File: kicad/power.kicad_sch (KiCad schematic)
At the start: 76 parts, among them J6 RTC Battery, U1 MIMXRT1171DVMAB, U8 TPS62086, U9 TPS62825, Y3 24MHz, Y4 32.768kHz

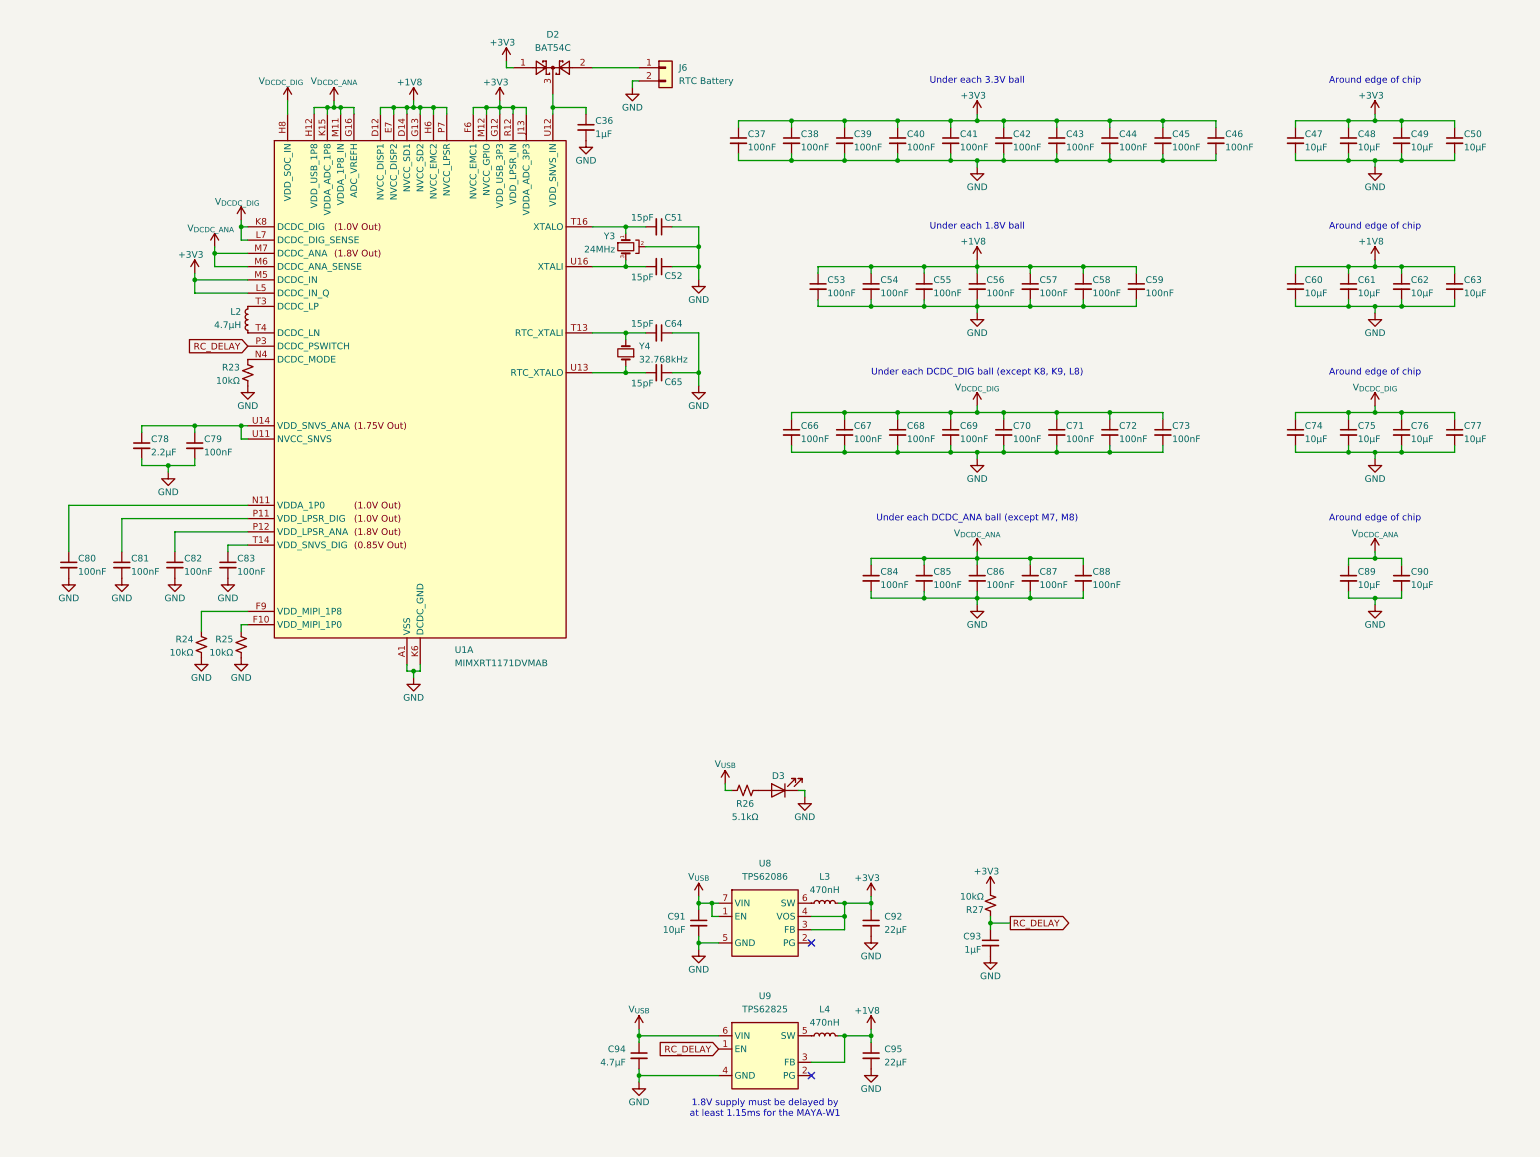
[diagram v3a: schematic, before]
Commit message: added inductor footprints
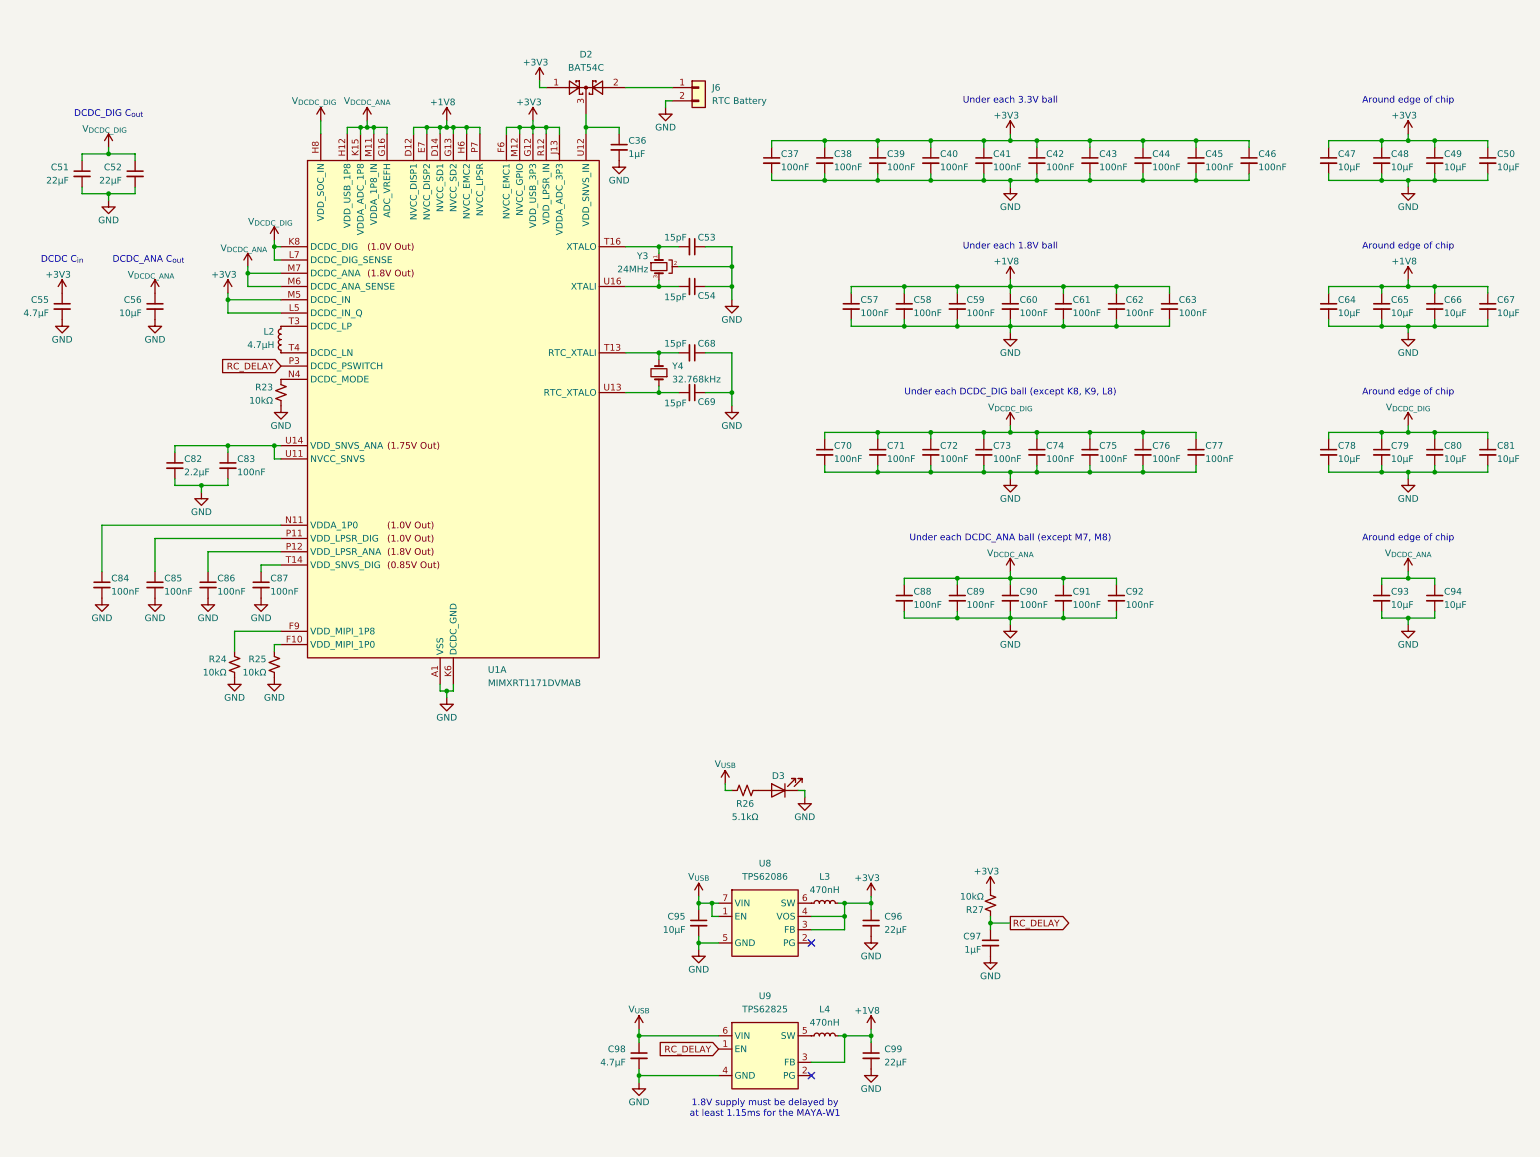
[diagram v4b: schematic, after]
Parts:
- added C51, C52: 22μF, Capacitor_SMD:C_0402_1005Metric, symbol Device:C_Small
- added C55: 4.7μF, Capacitor_SMD:C_0201_0603Metric, symbol Device:C_Small
- added C56: 10μF, Capacitor_SMD:C_0201_0603Metric, symbol Device:C_Small
- C53: renamed from C51; footprint Capacitor_SMD:C_0402_1005Metric -> Capacitor_SMD:C_0201_0603Metric
- C54: renamed from C52; footprint Capacitor_SMD:C_0402_1005Metric -> Capacitor_SMD:C_0201_0603Metric
- C60: renamed from C56; footprint Capacitor_SMD:C_0201_0603Metric -> Capacitor_SMD:C_0402_1005Metric
- C61: renamed from C57; footprint Capacitor_SMD:C_0201_0603Metric -> Capacitor_SMD:C_0402_1005Metric
- C62: renamed from C58; footprint Capacitor_SMD:C_0201_0603Metric -> Capacitor_SMD:C_0402_1005Metric
- C63: renamed from C59; footprint Capacitor_SMD:C_0201_0603Metric -> Capacitor_SMD:C_0402_1005Metric
- C66: renamed from C62; footprint Capacitor_SMD:C_0402_1005Metric -> Capacitor_SMD:C_0201_0603Metric
- C67: renamed from C63; footprint Capacitor_SMD:C_0402_1005Metric -> Capacitor_SMD:C_0201_0603Metric
- C68: renamed from C64; footprint Capacitor_SMD:C_0402_1005Metric -> Capacitor_SMD:C_0201_0603Metric
- C69: renamed from C65; footprint Capacitor_SMD:C_0402_1005Metric -> Capacitor_SMD:C_0201_0603Metric
- C74: renamed from C70; footprint Capacitor_SMD:C_0201_0603Metric -> Capacitor_SMD:C_0402_1005Metric
- C75: renamed from C71; footprint Capacitor_SMD:C_0201_0603Metric -> Capacitor_SMD:C_0402_1005Metric
- C76: renamed from C72; footprint Capacitor_SMD:C_0201_0603Metric -> Capacitor_SMD:C_0402_1005Metric
- C77: renamed from C73; footprint Capacitor_SMD:C_0201_0603Metric -> Capacitor_SMD:C_0402_1005Metric
- C78: renamed from C74; footprint Capacitor_SMD:C_0402_1005Metric -> (none)
- C79: renamed from C75; footprint Capacitor_SMD:C_0402_1005Metric -> Capacitor_SMD:C_0201_0603Metric
- C80: renamed from C76; footprint Capacitor_SMD:C_0402_1005Metric -> Capacitor_SMD:C_0201_0603Metric
- C81: renamed from C77; footprint Capacitor_SMD:C_0402_1005Metric -> Capacitor_SMD:C_0201_0603Metric
- C82: renamed from C78; footprint (none) -> Capacitor_SMD:C_0201_0603Metric
- C89: renamed from C85; footprint Capacitor_SMD:C_0201_0603Metric -> Capacitor_SMD:C_0402_1005Metric
- C90: renamed from C86; footprint Capacitor_SMD:C_0201_0603Metric -> Capacitor_SMD:C_0402_1005Metric
- C91: renamed from C87; footprint Capacitor_SMD:C_0201_0603Metric -> Capacitor_SMD:C_0402_1005Metric
- C92: renamed from C88; footprint Capacitor_SMD:C_0201_0603Metric -> (none)
- C93: renamed from C89; footprint Capacitor_SMD:C_0402_1005Metric -> (none)
- C94: renamed from C90; footprint Capacitor_SMD:C_0402_1005Metric -> (none)
- C95: renamed from C91; footprint Capacitor_SMD:C_0402_1005Metric -> (none)
- L2: footprint (none) -> project_footprints:SDCL1V4018
- L3, L4: footprint (none) -> project_footprints:L_0806
- renumbered C53 to C57, C54 to C58, C55 to C59, C60 to C64, C61 to C65, C66 to C70, C67 to C71, C68 to C72, C69 to C73, C79 to C83, C80 to C84, C81 to C85, C82 to C86, C83 to C87, C84 to C88, C92 to C96, C93 to C97, C94 to C98, C95 to C99
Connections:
- net +3V3: now also C55.1
- net GND: now also C51.2, C52.2, C55.2, C56.2
- net V_{DCDC_ANA}: now also C56.1
- net V_{DCDC_DIG}: now also C51.1, C52.1
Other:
- note added: "DCDC C_{in}"
- note added: "DCDC_ANA C_{out}"
- note added: "DCDC_DIG C_{out}"
- moved on the sheet: C36, C37, C38, C39, C40, C41, C42, C43, C44, C45, C46, C47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

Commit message: reworked bypass capacitors for MIMXRT1171DVMAB
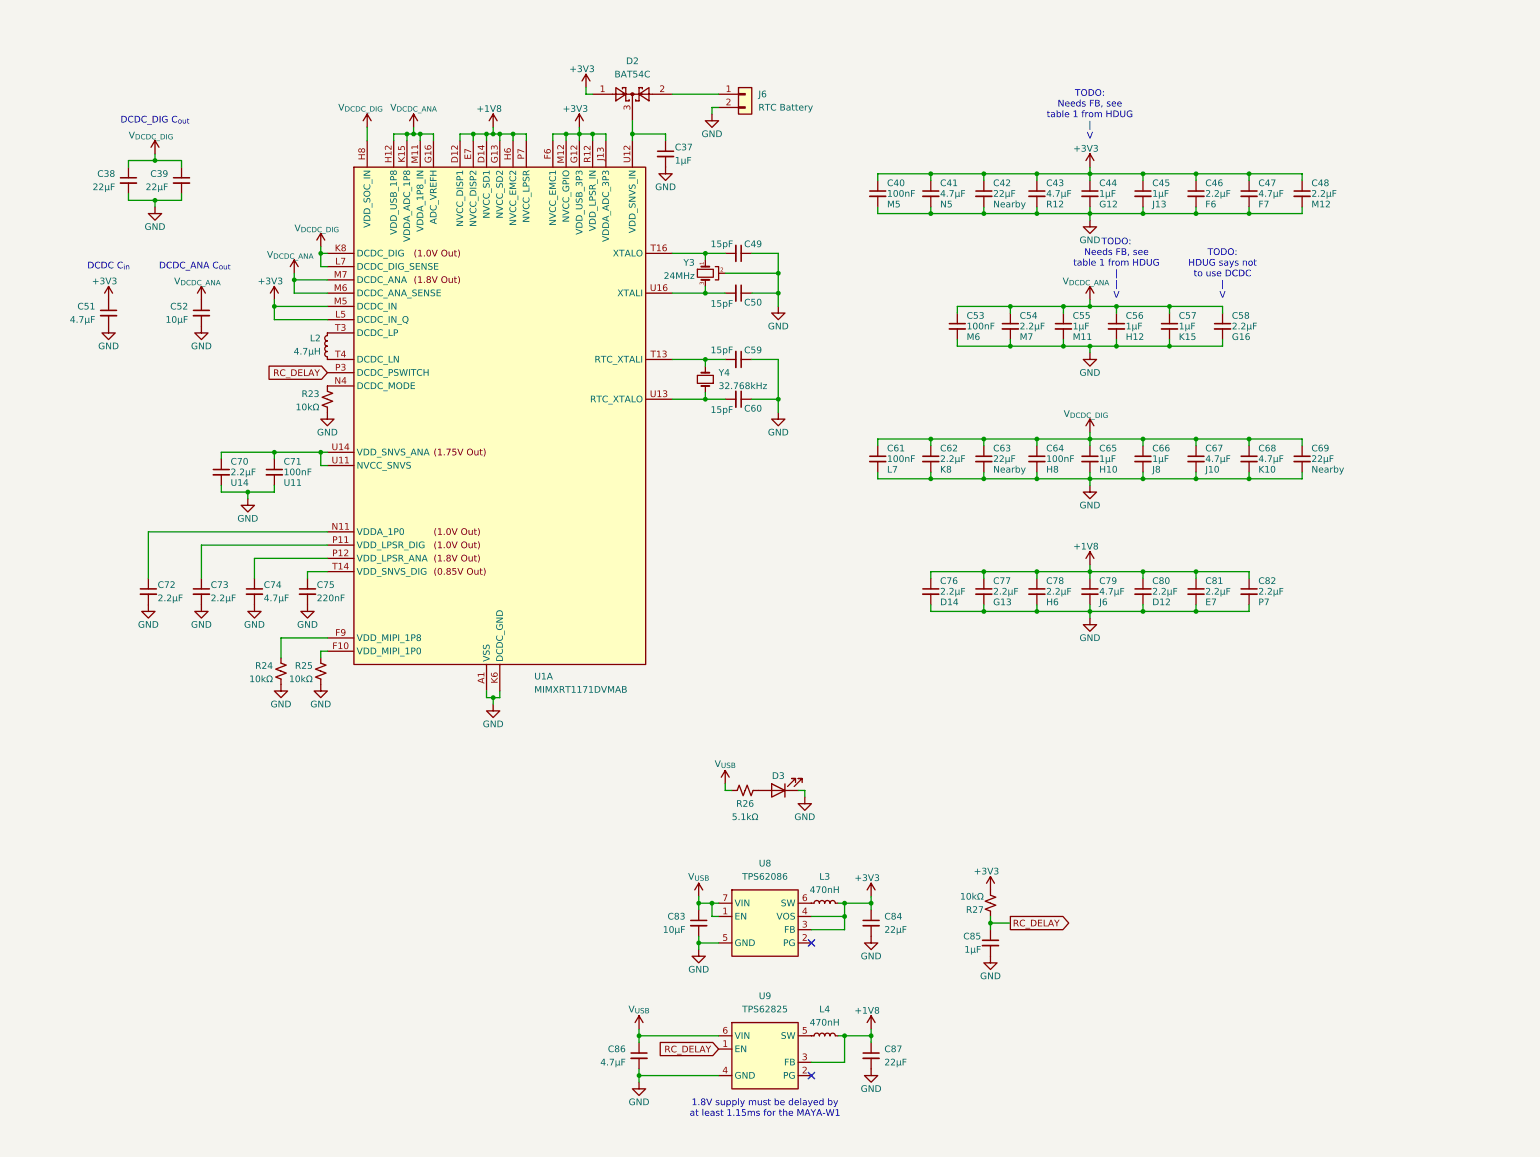
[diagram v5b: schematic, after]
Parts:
- removed C37, C38, C39, C59, C72, C83, C85, C88: 100nF, Capacitor_SMD:C_0201_0603Metric, symbol Device:C_Small
- removed C49, C50: 10μF, Capacitor_SMD:C_0402_1005Metric, symbol Device:C_Small
- removed C60, C74, C75, C89, C90, C91: 100nF, Capacitor_SMD:C_0402_1005Metric, symbol Device:C_Small
- removed C92: 100nF, symbol Device:C_Small
- removed C93, C94: 10μF, symbol Device:C_Small
- added C53: 100nF, symbol Device:C_Small
- added C54: 2.2μF, symbol Device:C_Small
- added C55, C56: 1μF, symbol Device:C_Small
- added C68: 4.7μF, symbol Device:C_Small
- added C69: 22μF, symbol Device:C_Small
- C37: renamed from C36; footprint Capacitor_SMD:C_0402_1005Metric -> (none)
- C38: renamed from C51; footprint Capacitor_SMD:C_0402_1005Metric -> (none)
- C39: renamed from C52; footprint Capacitor_SMD:C_0402_1005Metric -> (none)
- C40, C71, C82: footprint Capacitor_SMD:C_0201_0603Metric -> (none)
- C41, C43: value 100nF -> 4.7μF; footprint Capacitor_SMD:C_0201_0603Metric -> (none)
- C42: value 100nF -> 22μF; footprint Capacitor_SMD:C_0201_0603Metric -> (none)
- C44, C45, C57: value 100nF -> 1μF; footprint Capacitor_SMD:C_0201_0603Metric -> (none)
- C46, C58, C70, C73: value 100nF -> 2.2μF; footprint Capacitor_SMD:C_0201_0603Metric -> (none)
- C47: value 10μF -> 4.7μF; footprint Capacitor_SMD:C_0402_1005Metric -> (none)
- C48: value 10μF -> 2.2μF; footprint Capacitor_SMD:C_0402_1005Metric -> (none)
- C49: renamed from C53; footprint Capacitor_SMD:C_0201_0603Metric -> Capacitor_SMD:C_0402_1005Metric
- C50: renamed from C54; footprint Capacitor_SMD:C_0201_0603Metric -> Capacitor_SMD:C_0402_1005Metric
- C51: renamed from C55; footprint Capacitor_SMD:C_0201_0603Metric -> (none)
- C52: renamed from C56; footprint Capacitor_SMD:C_0201_0603Metric -> Capacitor_SMD:C_0402_1005Metric
- C59: renamed from C68; footprint Capacitor_SMD:C_0201_0603Metric -> Capacitor_SMD:C_0402_1005Metric
- C60: renamed from C69; footprint Capacitor_SMD:C_0201_0603Metric -> Capacitor_SMD:C_0402_1005Metric
- C61: footprint Capacitor_SMD:C_0402_1005Metric -> (none)
- C62, C76, C77: value 100nF -> 2.2μF; footprint Capacitor_SMD:C_0402_1005Metric -> (none)
- C63: value 100nF -> 22μF; footprint Capacitor_SMD:C_0402_1005Metric -> (none)
- C64: value 10μF -> 100nF; footprint Capacitor_SMD:C_0402_1005Metric -> (none)
- C65: value 10μF -> 1μF; footprint Capacitor_SMD:C_0402_1005Metric -> (none)
- C66: value 10μF -> 1μF; footprint Capacitor_SMD:C_0201_0603Metric -> (none)
- C67, C79: value 10μF -> 4.7μF; footprint Capacitor_SMD:C_0201_0603Metric -> (none)
- C72: renamed from C84; value 100nF -> 2.2μF
- C74: renamed from C86; value 100nF -> 4.7μF; footprint Capacitor_SMD:C_0201_0603Metric -> (none)
- C75: renamed from C87; value 100nF -> 220nF
- C78: value 10μF -> 2.2μF
- C80, C81: value 10μF -> 2.2μF; footprint Capacitor_SMD:C_0201_0603Metric -> (none)
- C83: renamed from C95; footprint (none) -> Capacitor_SMD:C_0402_1005Metric
- renumbered C96 to C84, C97 to C85, C98 to C86, C99 to C87
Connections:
- net +1V8: now also C76.1, C77.1, C78.1, C79.1, C80.1, C81.1, C82.1; no longer C57.1, C58.1, C61.1, C62.1, C63.1, C64.1, C65.1, C66.1, C67.1
- net GND: now also C53.2, C54.2, C55.2, C56.2, C68.2, C69.2
- net V_{DCDC_ANA}: now also C57.1, C58.1, C53.1, C54.1, C55.1, C56.1
- net V_{DCDC_DIG}: now also C61.1, C62.1, C63.1, C64.1, C65.1, C66.1, C67.1, C68.1, C69.1; no longer C70.1, C71.1, C73.1, C76.1, C77.1, C78.1, C79.1, C80.1, C81.1
- net at U1.P11 (VDD_LPSR_DIG): now also C73.1
- net at U1.U11 (NVCC_SNVS), U1.U14 (VDD_SNVS_ANA): now also C70.1, C71.1; no longer C82.1
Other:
- note added: "TODO: HDUG says not to use DCDC | V"
- note added: "TODO: Needs FB, see table 1 from HDUG | V"
- note added: "TODO: Needs FB, see table 1 from HDUG | | V"
- note removed: "Around edge of chip"
- note removed: "Under each 1.8V ball"
- note removed: "Under each 3.3V ball"
- note removed: "Under each DCDC_ANA ball (except M7, M8)"
- note removed: "Under each DCDC_DIG ball (except K8, K9, L8)"
- moved on the sheet: C37, C38, C39, C49, C50, C51, C52, C59, C60, C72, C74, C75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

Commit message: moved ADC_VREFH to +1V8 rail
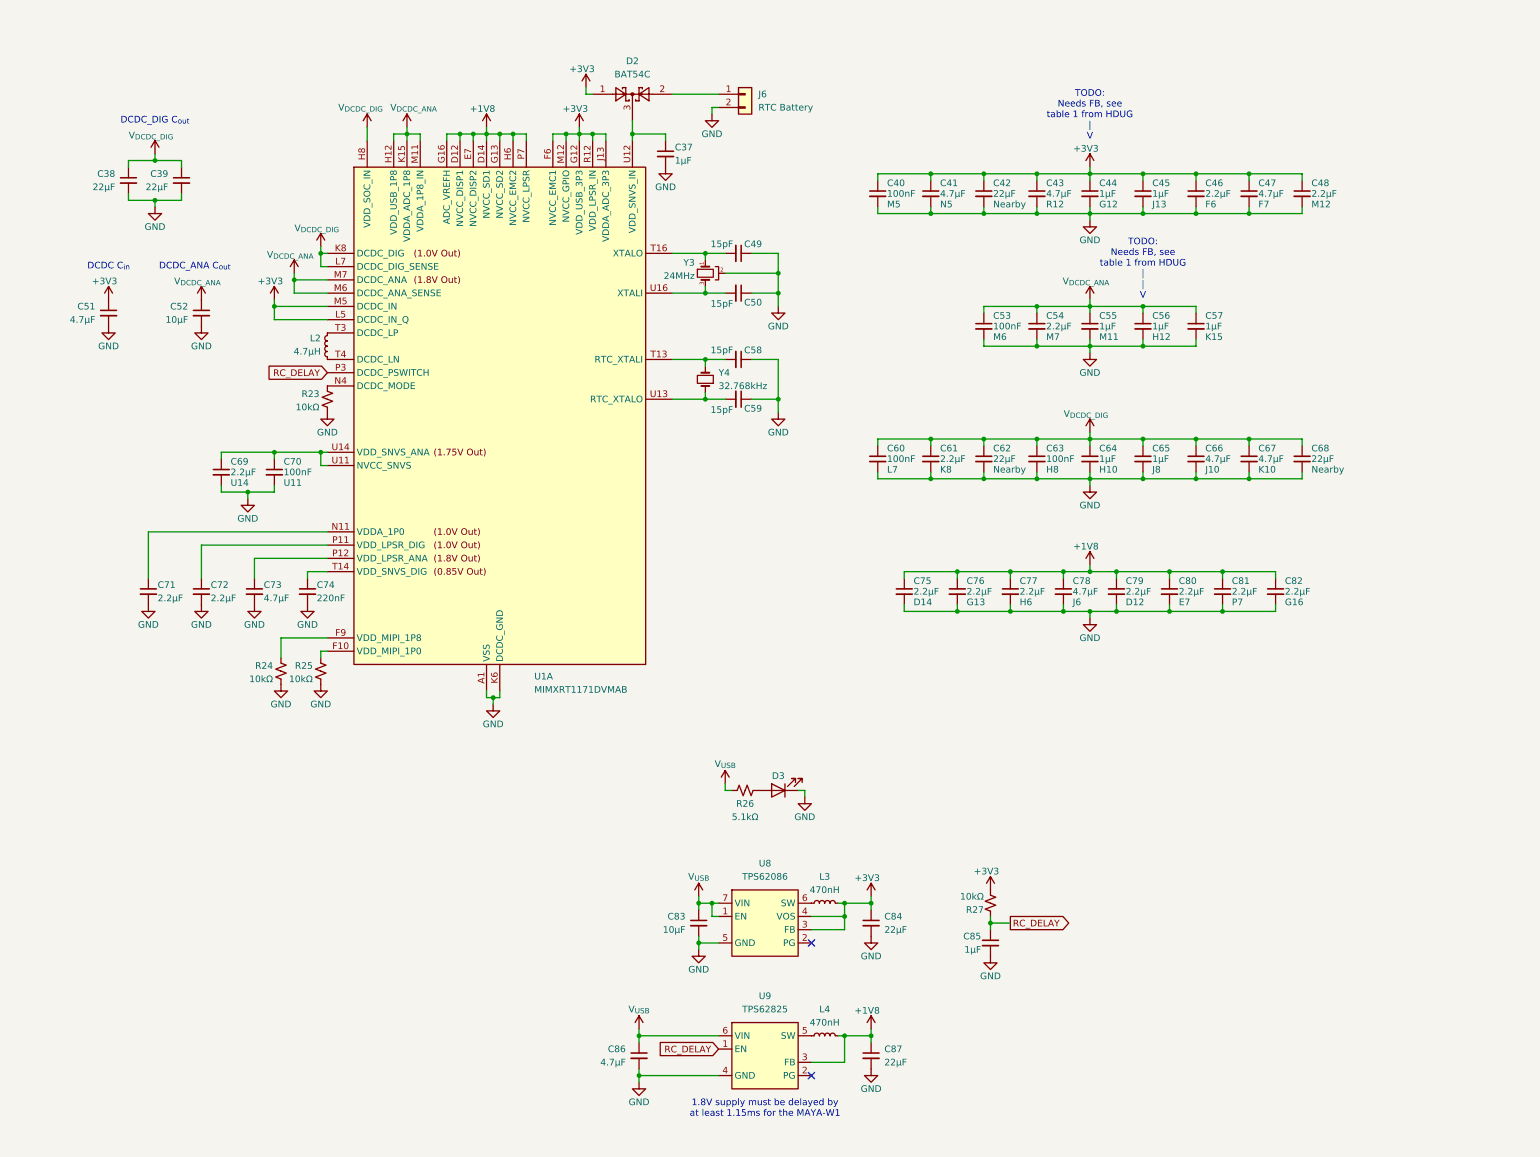
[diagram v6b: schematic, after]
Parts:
- removed C58: 2.2μF, symbol Device:C_Small
- added C82: 2.2μF, symbol Device:C_Small
- U1: footprint project_footprints:MIMXRT1171DVMAB -> Package_BGA:MAPBGA-289_14x14mm_Layout17x17_P0.8mm
- renumbered C59 to C58, C60 to C59, C61 to C60, C62 to C61, C63 to C62, C64 to C63, C65 to C64, C66 to C65, C67 to C66, C68 to C67, C69 to C68, C70 to C69, C71 to C70, C72 to C71, C73 to C72, C74 to C73, C75 to C74, C76 to C75, C77 to C76, C78 to C77, C79 to C78, C80 to C79, C81 to C80, C82 to C81
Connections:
- net +1V8: now also U1.G16 (ADC_VREFH), C82.1
- net GND: now also C82.2
- net V_{DCDC_ANA}: no longer U1.G16 (ADC_VREFH)
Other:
- note removed: "TODO: HDUG says not to use DCDC | V"
- moved on the sheet: C53, C54, C55, C56, C57, C75, C76, C77, C78, C79, C80, C81
